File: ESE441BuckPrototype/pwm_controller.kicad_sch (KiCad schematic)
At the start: 46 parts

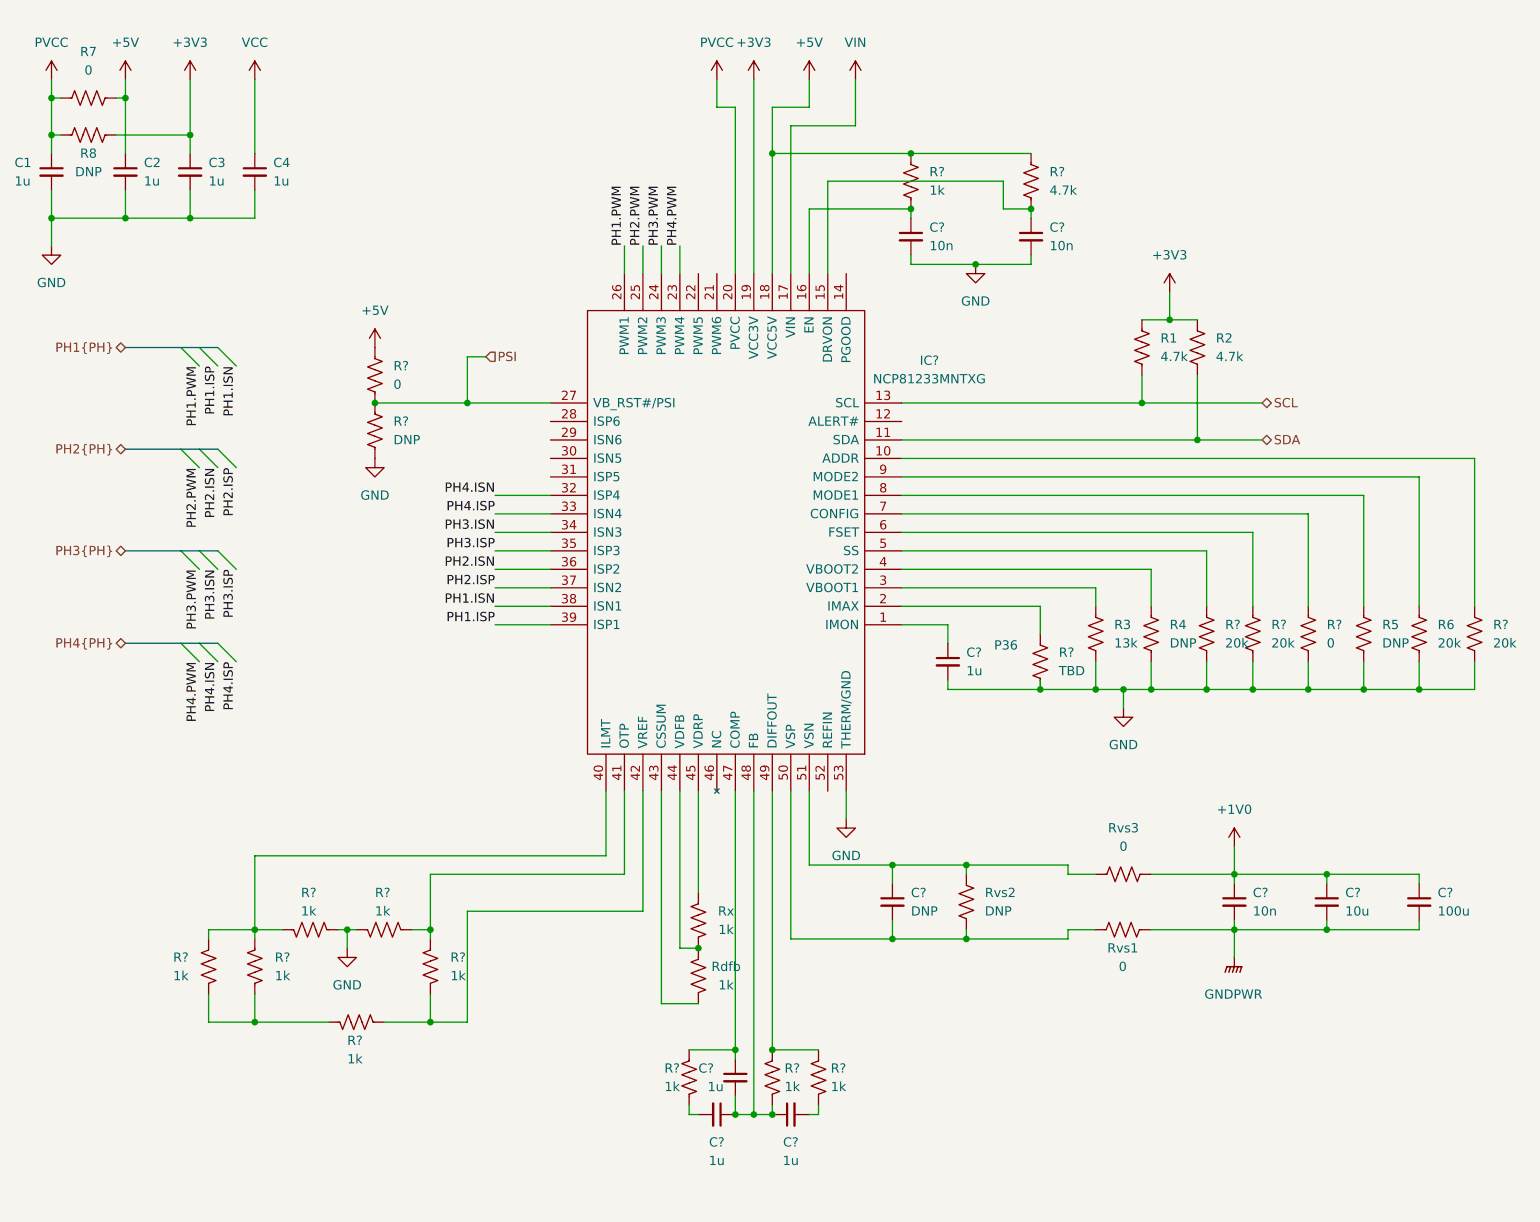
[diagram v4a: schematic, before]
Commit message: Set feedback and compensation network values
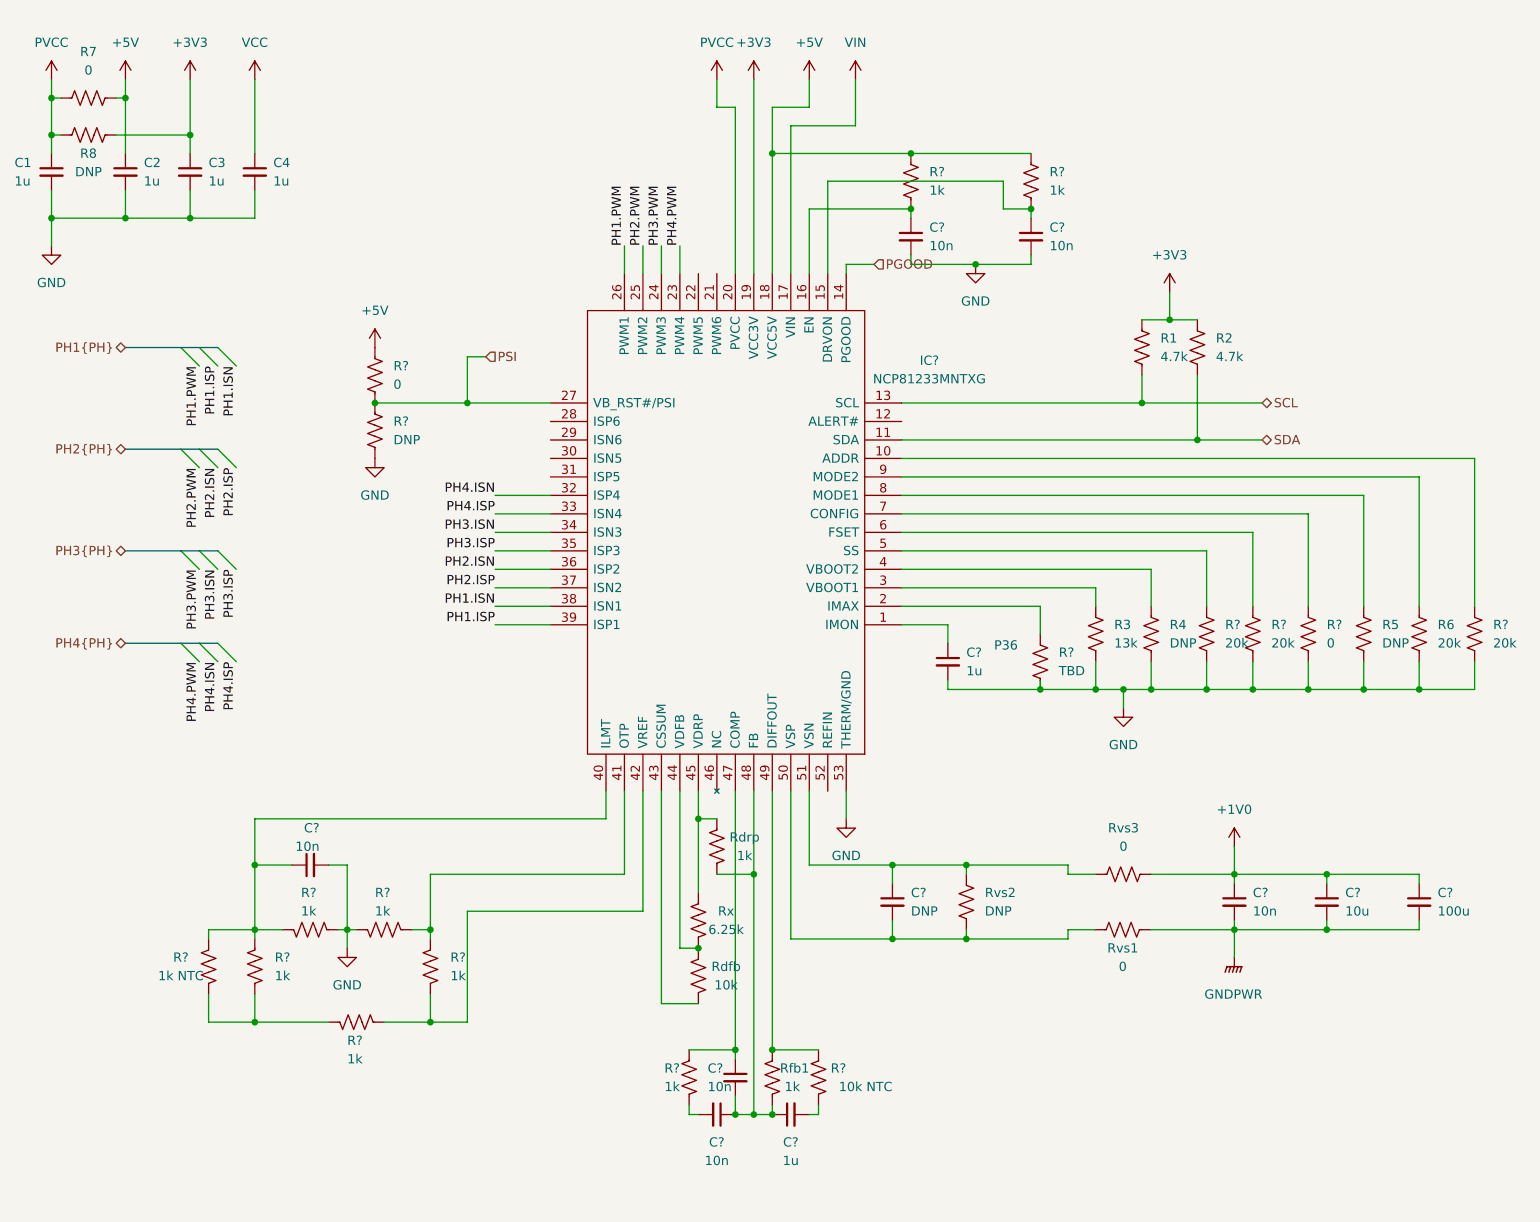
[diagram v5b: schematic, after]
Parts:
- added C?: 10n, symbol Device:C_Small
- added Rdrp: 1k, Resistor_SMD:R_0603_1608Metric, symbol Device:R_US
- C? (x2): value 1u -> 10n
- R?: value 4.7k -> 1k
- R?: value 1k -> 10k NTC
- R?: value 1k -> 1k NTC
- Rdfb: value 1k -> 10k
- Rx: value 1k -> 6.25k
- gave numbers to parts that had none: 1
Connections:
- net GND: now also C?.2
- net at C?.1, C?.1, C?.2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: now also Rdrp.1
- net at IC?.45 (VDRP), Rx.2: now also Rdrp.2
- net at IC?.40 (ILMT), R?.2, R?.2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: now also C?.1
- net PGOOD: now reaches IC?.14 (PGOOD)
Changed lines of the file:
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@@
   (junction (at 149.86 132.08) (diameter 0) (color 0 0 0 0)
   )
+  (junction (at 52.07 132.08) (diameter 0) (color 0 0 0 0)
+  )
   (junction (at 189.23 107.95) (diameter 0) (color 0 0 0 0)
   )
+  (junction (at 120.65 133.35) (diameter 0) (color 0 0 0 0)
+  )
   (junction (at 24.13 31.75) (diameter 0) (color 0 0 0 0)
   )
@@
   (junction (at 118.11 166.37) (diameter 0) (color 0 0 0 0)
   )
+  (junction (at 113.03 125.73) (diameter 0) (color 0 0 0 0)
+  )
   (junction (at 76.2 153.67) (diameter 0) (color 0 0 0 0)
   )
@@
     (stroke (width 0) (type default) (color 0 0 0 0))
   )
+  (wire (pts (xy 113.03 125.73) (xy 113.03 135.89))
+    (stroke (width 0) (type default) (color 0 0 0 0))
+  )
   (wire (pts (xy 160.02 100.33) (xy 160.02 96.52))
     (stroke (width 0) (type default) (color 0 0 0 0))
@@
     (stroke (width 0) (type default) (color 0 0 0 0))
   )
-  (wire (pts (xy 120.65 121.92) (xy 120.65 166.37))
+  (wire (pts (xy 120.65 121.92) (xy 120.65 133.35))
     (stroke (width 0) (type default) (color 0 0 0 0))
   )
@@
     (stroke (width 0) (type default) (color 0 0 0 0))
   )
-  (wire (pts (xy 52.07 140.97) (xy 52.07 130.81))
+  (wire (pts (xy 52.07 125.73) (xy 52.07 132.08))
     (stroke (width 0) (type default) (color 0 0 0 0))
   )
@@
     (stroke (width 0) (type default) (color 0 0 0 0))
   )
-  (wire (pts (xy 113.03 121.92) (xy 113.03 135.89))
+  (wire (pts (xy 113.03 121.92) (xy 113.03 125.73))
     (stroke (width 0) (type default) (color 0 0 0 0))
   )
@@
     (stroke (width 0) (type default) (color 0 0 0 0))
   )
+  (wire (pts (xy 120.65 133.35) (xy 120.65 166.37))
+    (stroke (width 0) (type default) (color 0 0 0 0))
+  )
   (bus (pts (xy 41.91 101.6) (xy 44.45 101.6))
     (stroke (width 0) (type default) (color 0 0 0 0))
   )
+  (wire (pts (xy 133.35 50.8) (xy 133.35 49.53))
+    (stroke (width 0) (type default) (color 0 0 0 0))
+  )
   (wire (pts (xy 181.61 64.77) (xy 181.61 73.66))
     (stroke (width 0) (type default) (color 0 0 0 0))
@@
     (stroke (width 0) (type default) (color 0 0 0 0))
   )
+  (wire (pts (xy 57.15 132.08) (xy 52.07 132.08))
+    (stroke (width 0) (type default) (color 0 0 0 0))
+  )
   (wire (pts (xy 167.64 104.14) (xy 167.64 107.95))
     (stroke (width 0) (type default) (color 0 0 0 0))
@@
     (stroke (width 0) (type default) (color 0 0 0 0))
   )
+  (wire (pts (xy 133.35 49.53) (xy 137.16 49.53))
+    (stroke (width 0) (type default) (color 0 0 0 0))
+  )
   (wire (pts (xy 73.66 140.97) (xy 76.2 140.97))
     (stroke (width 0) (type default) (color 0 0 0 0))
@@
     (stroke (width 0) (type default) (color 0 0 0 0))
   )
-  (wire (pts (xy 100.33 121.92) (xy 100.33 130.81))
+  (wire (pts (xy 100.33 121.92) (xy 100.33 125.73))
     (stroke (width 0) (type default) (color 0 0 0 0))
   )
@@
     (stroke (width 0) (type default) (color 0 0 0 0))
   )
-  (wire (pts (xy 52.07 130.81) (xy 100.33 130.81))
+  (wire (pts (xy 52.07 125.73) (xy 100.33 125.73))
     (stroke (width 0) (type default) (color 0 0 0 0))
   )
@@
     (stroke (width 0) (type default) (color 0 0 0 0))
   )
+  (wire (pts (xy 64.77 132.08) (xy 64.77 140.97))
+    (stroke (width 0) (type default) (color 0 0 0 0))
+  )
   (wire (pts (xy 68.58 68.58) (xy 81.28 68.58))
     (stroke (width 0) (type default) (color 0 0 0 0))
@@
     (stroke (width 0) (type default) (color 0 0 0 0))
   )
+  (wire (pts (xy 113.03 125.73) (xy 115.57 125.73))
+    (stroke (width 0) (type default) (color 0 0 0 0))
+  )
   (wire (pts (xy 186.69 133.35) (xy 186.69 134.62))
     (stroke (width 0) (type default) (color 0 0 0 0))
@@
     (stroke (width 0) (type default) (color 0 0 0 0))
   )
+  (wire (pts (xy 115.57 133.35) (xy 120.65 133.35))
+    (stroke (width 0) (type default) (color 0 0 0 0))
+  )
   (wire (pts (xy 140.97 83.82) (xy 196.85 83.82))
     (stroke (width 0) (type default) (color 0 0 0 0))
   )
+  (wire (pts (xy 52.07 132.08) (xy 52.07 140.97))
+    (stroke (width 0) (type default) (color 0 0 0 0))
+  )
   (wire (pts (xy 167.64 107.95) (xy 171.45 107.95))
     (stroke (width 0) (type default) (color 0 0 0 0))
@@
   )
   (wire (pts (xy 111.76 157.48) (xy 118.11 157.48))
+    (stroke (width 0) (type default) (color 0 0 0 0))
+  )
+  (wire (pts (xy 62.23 132.08) (xy 64.77 132.08))
     (stroke (width 0) (type default) (color 0 0 0 0))
   )
@@
   )
   (hierarchical_label "SCL" (shape bidirectional) (at 190.5 68.58 0)
+    (effects (font (size 1.27 1.27)) (justify left))
+  )
+  (hierarchical_label "PGOOD" (shape input) (at 137.16 49.53 0)
     (effects (font (size 1.27 1.27)) (justify left))
   )
@@
     (in_bom yes) (on_board yes)
     (property "Reference" "Rdfb" (id 0) (at 116.84 146.05 0))
-    (property "Value" "1k" (id 1) (at 116.84 148.59 0))
+    (property "Value" "10k" (id 1) (at 116.84 148.59 0))
     (property "Footprint" "Resistor_SMD:R_0603_1608Metric" (id 2) (at 114.046 147.066 90)
       (effects (font (size 1.27 1.27)) hide)
@@
       (effects (font (size 1.27 1.27)) (justify left))
     )
-    (property "Value" "4.7k" (id 1) (at 161.29 39.3699 0)
+    (property "Value" "1k" (id 1) (at 161.29 39.3699 0)
       (effects (font (size 1.27 1.27)) (justify left))
     )
@@
       (effects (font (size 1.27 1.27)) (justify left))
     )
-    (property "Value" "1k" (id 1) (at 133.35 162.5599 0)
+    (property "Value" "10k NTC" (id 1) (at 139.7 162.5599 0)
       (effects (font (size 1.27 1.27)) (justify left))
     )
@@
     )
     (property "Datasheet" "~" (id 3) (at 129.54 161.29 0)
+      (effects (font (size 1.27 1.27)) hide)
+    )
+    (pin "1")
+    (pin "2")
+  )
+  (symbol (lib_id "Device:R_US") (at 115.57 129.54 0) (mirror x) (unit 1)
+    (in_bom yes) (on_board yes)
+    (property "Reference" "Rdrp" (id 0) (at 119.38 128.27 0))
+    (property "Value" "1k" (id 1) (at 119.38 130.81 0))
+    (property "Footprint" "Resistor_SMD:R_0603_1608Metric" (id 2) (at 116.586 129.286 90)
+      (effects (font (size 1.27 1.27)) hide)
+    )
+    (property "Datasheet" "~" (id 3) (at 115.57 129.54 0)
       (effects (font (size 1.27 1.27)) hide)
     )
@@
   (symbol (lib_id "Device:R_US") (at 123.19 161.29 0) (mirror y) (unit 1)
     (in_bom yes) (on_board yes)
-    (property "Reference" "R?" (id 0) (at 127 160.0199 0)
+    (property "Reference" "Rfb1" (id 0) (at 128.27 160.0199 0)
       (effects (font (size 1.27 1.27)) (justify left))
     )
@@
     (in_bom yes) (on_board yes)
     (property "Reference" "Rx" (id 0) (at 116.84 138.43 0))
-    (property "Value" "1k" (id 1) (at 116.84 140.97 0))
+    (property "Value" "6.25k" (id 1) (at 116.84 140.97 0))
     (property "Footprint" "Resistor_SMD:R_0603_1608Metric" (id 2) (at 114.046 139.446 90)
       (effects (font (size 1.27 1.27)) hide)
@@
     (pin "1")
   )
+  (symbol (lib_id "Device:C_Small") (at 59.69 132.08 90) (unit 1)
+    (in_bom yes) (on_board yes)
+    (property "Reference" "C?" (id 0) (at 60.9662 127 90)
+      (effects (font (size 1.27 1.27)) (justify left))
+    )
+    (property "Value" "10n" (id 1) (at 60.9662 129.54 90)
+      (effects (font (size 1.27 1.27)) (justify left))
+    )
+    (property "Footprint" "" (id 2) (at 59.69 132.08 0)
+      (effects (font (size 1.27 1.27)) hide)
+    )
+    (property "Datasheet" "~" (id 3) (at 59.69 132.08 0)
+      (effects (font (size 1.27 1.27)) hide)
+    )
+    (pin "1")
+    (pin "2")
+  )
   (symbol (lib_id "Device:R_US") (at 68.58 64.77 0) (unit 1)
     (in_bom yes) (on_board yes) (fields_autoplaced)
@@
   (symbol (lib_id "Device:C_Small") (at 118.11 161.29 0) (unit 1)
     (in_bom yes) (on_board yes)
-    (property "Reference" "C?" (id 0) (at 113.03 160.0262 0)
-      (effects (font (size 1.27 1.27)) (justify left))
-    )
-    (property "Value" "1u" (id 1) (at 114.3 162.5662 0)
+    (property "Reference" "C?" (id 0) (at 114.3 160.0262 0)
+      (effects (font (size 1.27 1.27)) (justify left))
+    )
+    (property "Value" "10n" (id 1) (at 114.3 162.5662 0)
       (effects (font (size 1.27 1.27)) (justify left))
     )
@@
     (in_bom yes) (on_board yes)
     (property "Reference" "C?" (id 0) (at 115.5636 170.18 90))
-    (property "Value" "1u" (id 1) (at 115.5636 172.72 90))
+    (property "Value" "10n" (id 1) (at 115.5636 172.72 90))
     (property "Footprint" "" (id 2) (at 115.57 166.37 0)
       (effects (font (size 1.27 1.27)) hide)
@@
     (in_bom yes) (on_board yes)
     (property "Reference" "R?" (id 0) (at 41.91 144.78 0))
-    (property "Value" "1k" (id 1) (at 41.91 147.32 0))
+    (property "Value" "1k NTC" (id 1) (at 41.91 147.32 0))
     (property "Footprint" "Resistor_SMD:R_0603_1608Metric" (id 2) (at 46.736 145.796 90)
       (effects (font (size 1.27 1.27)) hide)

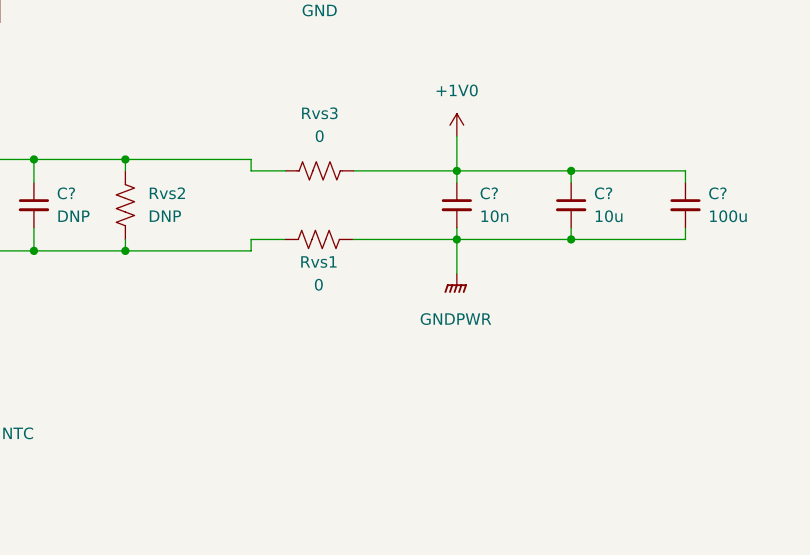
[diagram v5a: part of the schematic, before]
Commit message: Values for current measuring network
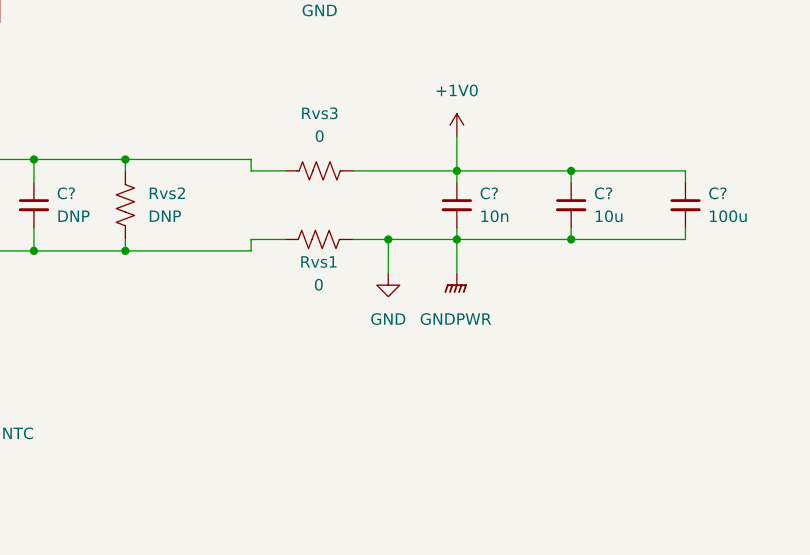
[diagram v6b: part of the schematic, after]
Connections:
- net GNDPWR is gone; now on net GND: C?.2, C?.2, C?.2, Rvs1.2
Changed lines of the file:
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@@
   (junction (at 151.13 49.53) (diameter 0) (color 0 0 0 0)
   )
+  (junction (at 179.07 140.97) (diameter 0) (color 0 0 0 0)
+  )
   (junction (at 196.85 107.95) (diameter 0) (color 0 0 0 0)
   )
@@
     (stroke (width 0) (type default) (color 0 0 0 0))
   )
-  (wire (pts (xy 175.1644 140.97) (xy 186.69 140.97))
+  (wire (pts (xy 175.1644 140.97) (xy 179.07 140.97))
     (stroke (width 0) (type default) (color 0 0 0 0))
   )
@@
     (stroke (width 0) (type default) (color 0 0 0 0))
   )
+  (wire (pts (xy 179.07 140.97) (xy 179.07 144.78))
+    (stroke (width 0) (type default) (color 0 0 0 0))
+  )
   (wire (pts (xy 100.33 121.92) (xy 100.33 125.73))
     (stroke (width 0) (type default) (color 0 0 0 0))
@@
   )
   (wire (pts (xy 186.69 140.97) (xy 199.39 140.97))
+    (stroke (width 0) (type default) (color 0 0 0 0))
+  )
+  (wire (pts (xy 179.07 140.97) (xy 186.69 140.97))
     (stroke (width 0) (type default) (color 0 0 0 0))
   )
@@
     (pin "2")
   )
+  (symbol (lib_id "power:GND") (at 179.07 144.78 0) (unit 1)
+    (in_bom yes) (on_board yes) (fields_autoplaced)
+    (property "Reference" "#PWR?" (id 0) (at 179.07 151.13 0)
+      (effects (font (size 1.27 1.27)) hide)
+    )
+    (property "Value" "GND" (id 1) (at 179.07 149.86 0))
+    (property "Footprint" "" (id 2) (at 179.07 144.78 0)
+      (effects (font (size 1.27 1.27)) hide)
+    )
+    (property "Datasheet" "" (id 3) (at 179.07 144.78 0)
+      (effects (font (size 1.27 1.27)) hide)
+    )
+    (pin "1")
+  )
   (symbol (lib_id "Device:C_Small") (at 34.29 36.83 0) (unit 1)
